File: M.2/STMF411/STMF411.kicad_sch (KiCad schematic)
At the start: 23 parts, among them M1 M.2_Key_E, Q1 2N7002, U1 LDK120PU-R_DFN6, U2 STM32F411CCUx, Y1 16 MHz

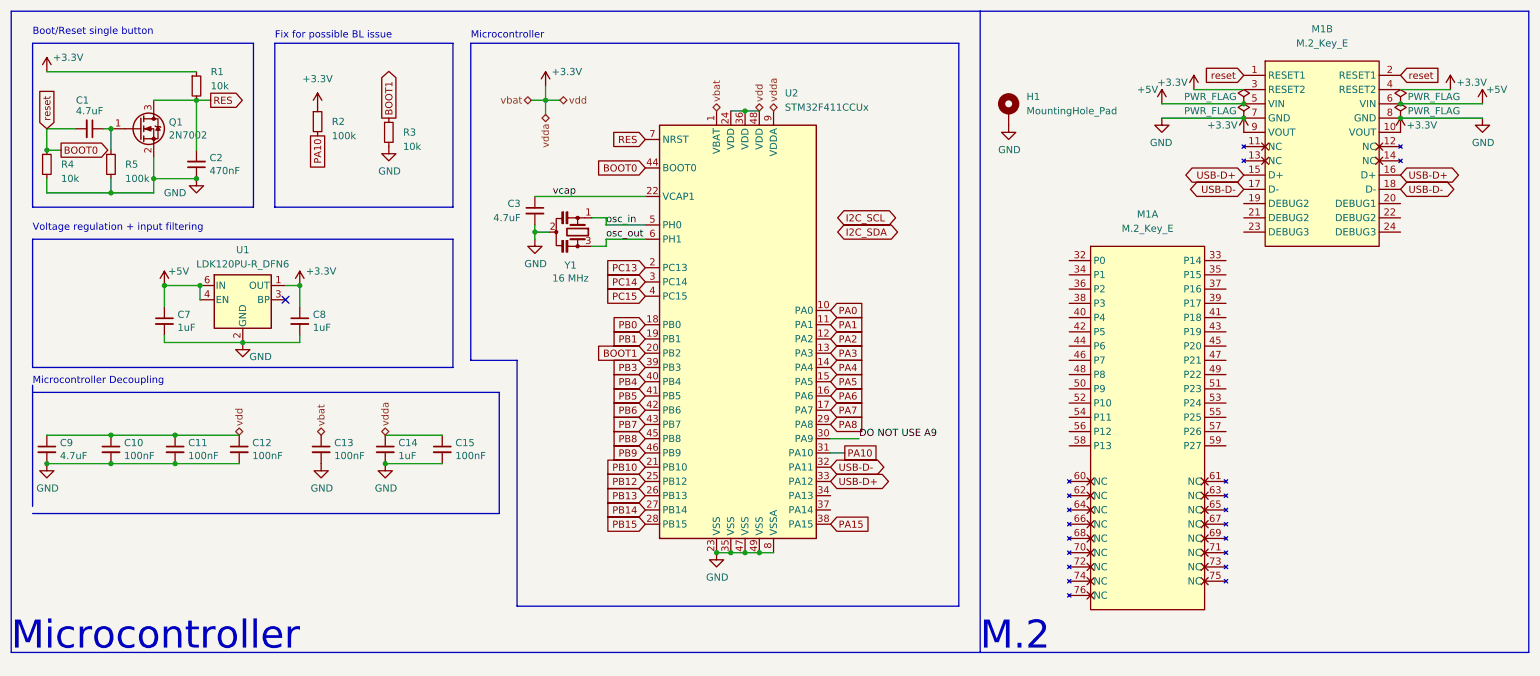
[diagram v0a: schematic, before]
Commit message: finish f411 and change it to key e
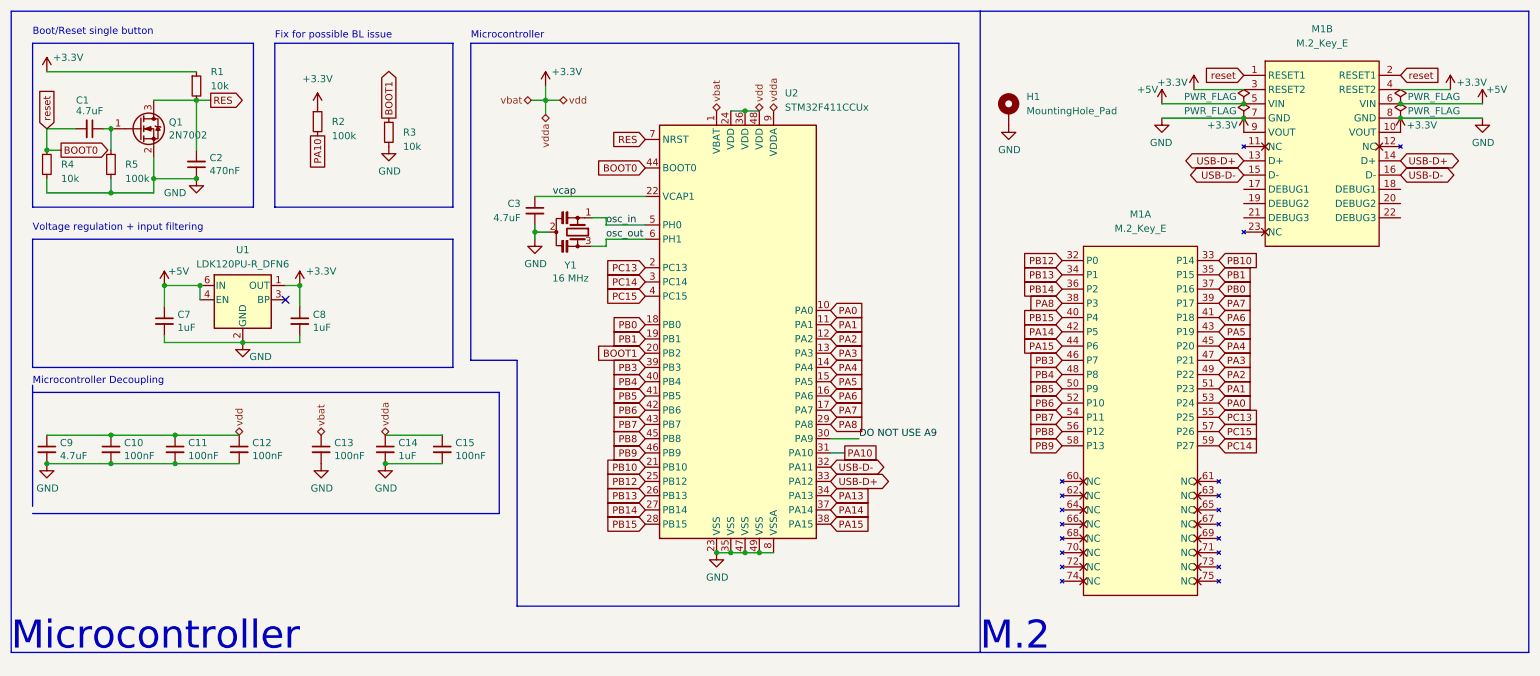
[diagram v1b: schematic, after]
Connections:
- net PA0: now also M1.53 (P24)
- net PA1: now also M1.51 (P23)
- net PA15: now also M1.44 (P6)
- net PA2: now also M1.49 (P22)
- net PA3: now also M1.47 (P21)
- net PA4: now also M1.45 (P20)
- net PA5: now also M1.43 (P19)
- net PA6: now also M1.41 (P18)
- net PA7: now also M1.39 (P17)
- net PA8: now also M1.38 (P3)
- net PB0: now also M1.37 (P16)
- net PB1: now also M1.35 (P15)
- net PB10: now also M1.33 (P14)
- net PB12: now also M1.32 (P0)
- net PB13: now also M1.34 (P1)
- net PB14: now also M1.36 (P2)
- net PB15: now also M1.40 (P4)
- net PB3: now also M1.46 (P7)
- net PB4: now also M1.48 (P8)
- net PB5: now also M1.50 (P9)
- net PB6: now also M1.52 (P10)
- net PB7: now also M1.54 (P11)
- net PB8: now also M1.56 (P12)
- net PB9: now also M1.58 (P13)
- net PC13: now also M1.55 (P25)
- net PC14: now also M1.59 (P27)
- net PC15: now also M1.57 (P26)
- net USB-D+: now also M1.13 (D+), M1.14 (D+); no longer M1.15 (D+), M1.16 (D+)
- net USB-D-: now also M1.15 (D-), M1.16 (D-); no longer M1.17 (D-), M1.18 (D-)
- net PA14: now reaches M1.42 (P5)
- net PA14: now also U2.37 (PA14)
- net PA13: now reaches U2.34 (PA13)
